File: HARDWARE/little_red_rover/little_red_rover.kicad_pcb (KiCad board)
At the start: 2 copper layers, 127.3 x 82.2 mm, 60 parts, among them J1 USB_C_Receptacle_USB2.0_14P, J2 Conn_01x04_Socket, J3 Conn_01x02_Socket, J4 Conn_01x02_Socket, J5 Conn_01x01_Socket, J6 Conn_01x01_Socket, J8 Conn_02x12_Odd_Even, SW1 SW_Push, SW2 SW_Push, SW3 SW_Push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

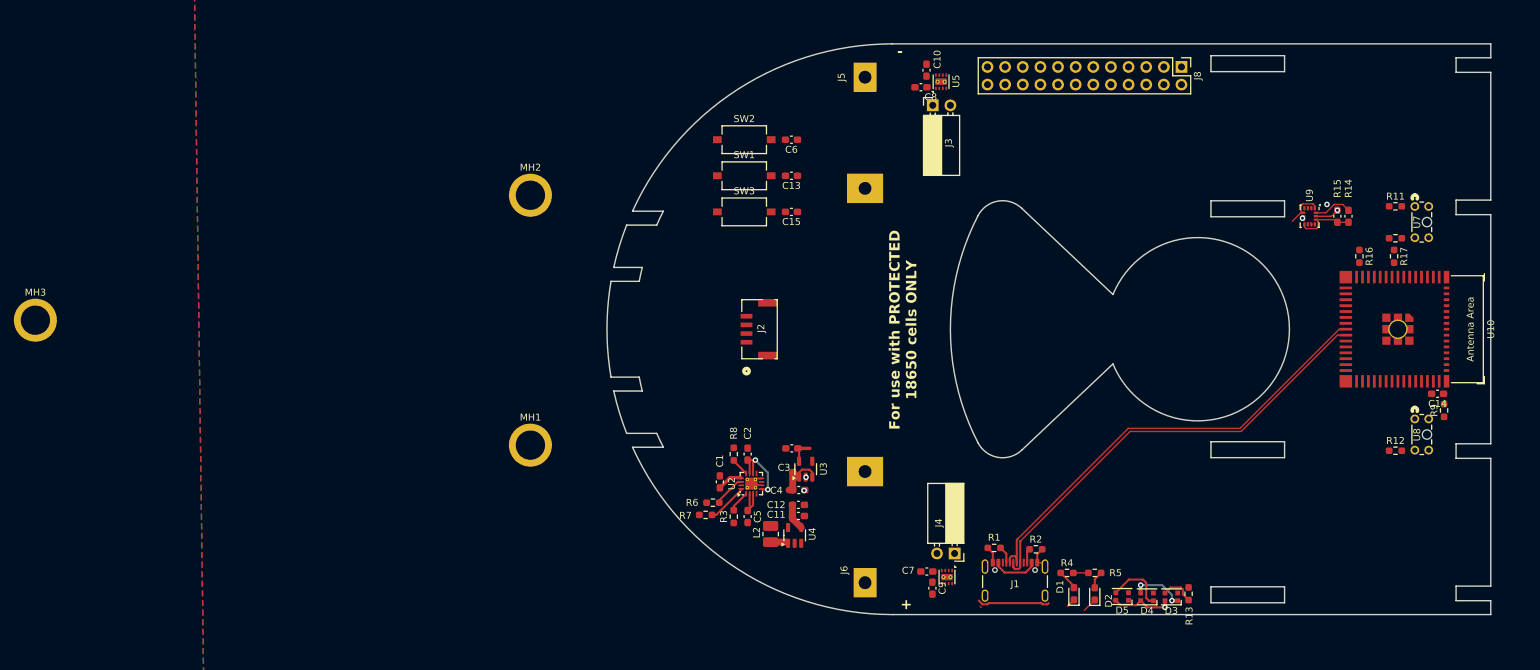
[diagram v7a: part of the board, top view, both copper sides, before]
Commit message: Route traces for v1.1
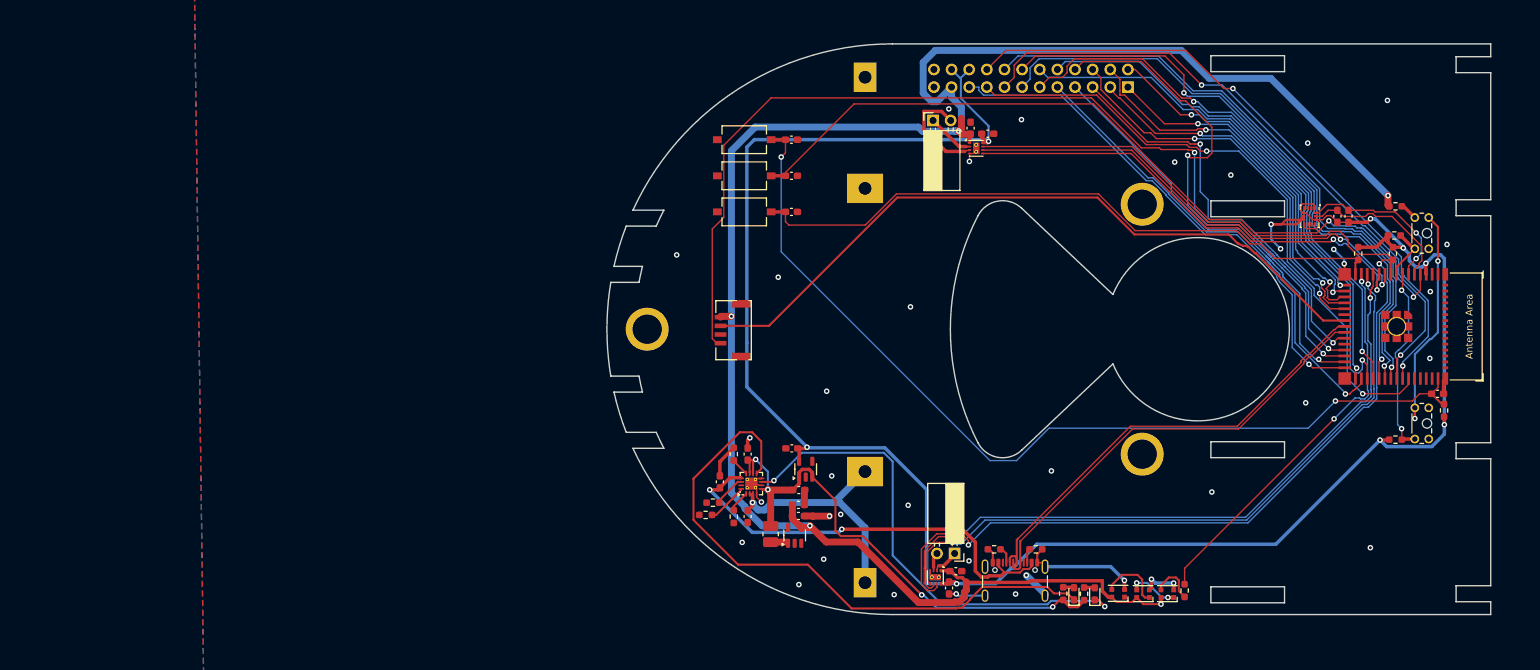
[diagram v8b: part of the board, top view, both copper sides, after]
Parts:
- J8: moved to B.Cu
- moved MH1 88.1 mm to (163.5, 117.9)
- moved MH2 88.1 mm to (163.5, 81.9)
- moved MH3 88.1 mm to (92.2, 99.9)
- moved C10 12.7 mm to (141.3, 71.7), turned to 0 degrees
- moved U5 10.8 mm to (139.6, 73.8), turned to 0 degrees
- moved C8 9.26 mm to (138.8, 70.9), turned to 90 degrees
- moved J8 8.24 mm to (161.5, 65.0), turned to 90 degrees
- moved C7 4.17 mm to (136.7, 134.8), turned to 0 degrees
- moved J2 3.74 mm to (104.7, 100.0)
- moved R5 3.38 mm to (155.2, 138.0), turned to -90 degrees
- moved R4 3.03 mm to (152.1, 138.0), turned to -90 degrees
- moved C9 2.40 mm to (135.7, 137.2)
- moved J3 2.18 mm to (133.4, 69.8)
- moved U6 1.68 mm to (133.7, 135.6)
- moved R12 1.60 mm to (200.0, 115.8)
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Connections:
- J2 pad 1: +3.3V -> /lidar_pwm
- J8 pad 1: /GPIO_12 -> /GPIO_13
- J8 pad 10: /GPIO_36 -> /GPIO_35
- J8 pad 11: /GPIO_37 -> /GPIO_38
- J8 pad 12: /GPIO_38 -> /GPIO_37
- J8 pad 13: /GPIO_39 -> /GPIO_40
- J8 pad 14: /GPIO_40 -> /GPIO_39
- J8 pad 15: /GPIO_41 -> /GPIO_42
- J8 pad 16: /GPIO_42 -> /GPIO_41
- J8 pad 17: /GPIO_43 -> /GPIO_44
- J8 pad 18: /GPIO_44 -> /GPIO_43
- J8 pad 19: /GPIO_47 -> /GPIO_48
- J8 pad 2: /GPIO_13 -> /GPIO_12
- J8 pad 20: /GPIO_48 -> +3.3V
- J8 pad 21: +3.3V -> +5V
- J8 pad 22: +5V -> +3.3V
- J8 pad 3: /GPIO_14 -> /GPIO_15
- J8 pad 4: /GPIO_15 -> /GPIO_14
- J8 pad 5: /GPIO_16 -> /GPIO_21
- J8 pad 6: /GPIO_21 -> /GPIO_16
- J8 pad 7: /GPIO_33 -> /GPIO_34
- J8 pad 8: /GPIO_34 -> /GPIO_33
- J8 pad 9: /GPIO_35 -> /GPIO_36
- U10 pad 27: /GPIO_47 -> /lidar_pwm
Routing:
- net +3.3V: track 17.7 -> 293.9 mm, vias 0 -> 8
- net +5V: track 13.1 -> 270.1 mm, vias 1 -> 5
- net /motor_sleep: track 0.00 -> 176.6 mm, vias 0 -> 2
- net /lidar_pwm: track 0.00 -> 145.3 mm, vias 0 -> 2
- net /chip_en: track 0.00 -> 133.8 mm, vias 0 -> 2
- net /boot: track 0.00 -> 115.3 mm, vias 0 -> 2
- net /lidar_tx: track 0.00 -> 104.8 mm
- net /right_motor_pwm_a: track 0.00 -> 98.7 mm, vias 0 -> 2
- net /right_motor_pwm_b: track 0.00 -> 97.0 mm, vias 1 -> 2
- net /GPIO_42: track 0.00 -> 94.3 mm, vias 0 -> 2
- net /reprovision: track 0.00 -> 94.2 mm
- net /GPIO_43: track 0.00 -> 93.8 mm, vias 0 -> 2
- net /GPIO_44: track 0.00 -> 90.4 mm, vias 0 -> 2
- net /GPIO_41: track 0.00 -> 89.9 mm, vias 0 -> 1
- net /GPIO_40: track 0.00 -> 89.1 mm, vias 0 -> 1
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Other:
- outline, holes or cut-outs redrawn
- board text removed: "+"
- board text removed: "-"
- board text removed: "For use with PROTECTED 18650 cells ONLY"
- board text removed: "little red rover v1.0"
